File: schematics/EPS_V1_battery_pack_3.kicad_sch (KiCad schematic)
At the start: 31 parts, among them U10 MP2672AGD-0000-Z, U11 MAX17205G+

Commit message: Fix NC pins, add 2 test points & silkscreen labels
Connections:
- net GND: now also U10.14 (SCL), U10.15 (SDA), U11.10 (AIN2), U11.9 (AIN1)
- no-connect marks 6 -> 2
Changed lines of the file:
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@@
 	)
 	(junction
+		(at 229.87 87.63)
+		(diameter 0)
+		(color 0 0 0 0)
+	)
+	(junction
+		(at 104.14 91.44)
+		(diameter 0)
+		(color 0 0 0 0)
+	)
+	(junction
 		(at 196.85 101.6)
 		(diameter 0)
@@
 	)
 	(junction
+		(at 104.14 88.9)
+		(diameter 0)
+		(color 0 0 0 0)
+	)
+	(junction
 		(at 58.42 67.31)
 		(diameter 0)
@@
 	)
 	(no_connect
-		(at 104.14 88.9)
-	)
-	(no_connect
-		(at 229.87 90.17)
-	)
-	(no_connect
-		(at 104.14 86.36)
-	)
-	(no_connect
 		(at 229.87 77.47)
 	)
-	(no_connect
-		(at 229.87 87.63)
-	)
 	(wire
 		(pts
@@
 	(wire
 		(pts
-			(xy 229.87 92.71) (xy 231.14 92.71)
-		)
-		(stroke
-			(width 0)
-			(type default)
-		)
-	)
-	(wire
-		(pts
 			(xy 104.14 81.28) (xy 116.84 81.28)
 		)
@@
 	(wire
 		(pts
+			(xy 229.87 95.25) (xy 229.87 92.71)
+		)
+		(stroke
+			(width 0)
+			(type default)
+		)
+	)
+	(wire
+		(pts
 			(xy 121.92 68.58) (xy 121.92 63.5)
 		)
@@
 	(wire
 		(pts
+			(xy 104.14 88.9) (xy 104.14 91.44)
+		)
+		(stroke
+			(width 0)
+			(type default)
+		)
+	)
+	(wire
+		(pts
 			(xy 267.97 82.55) (xy 265.43 82.55)
 		)
@@
 	(wire
 		(pts
+			(xy 229.87 95.25) (xy 232.41 95.25)
+		)
+		(stroke
+			(width 0)
+			(type default)
+		)
+	)
+	(wire
+		(pts
 			(xy 62.23 81.28) (xy 63.5 81.28)
 		)
@@
 	(wire
 		(pts
+			(xy 229.87 87.63) (xy 229.87 90.17)
+		)
+		(stroke
+			(width 0)
+			(type default)
+		)
+	)
+	(wire
+		(pts
 			(xy 118.11 104.14) (xy 120.65 104.14)
 		)
@@
 	(wire
 		(pts
+			(xy 104.14 86.36) (xy 104.14 88.9)
+		)
+		(stroke
+			(width 0)
+			(type default)
+		)
+	)
+	(wire
+		(pts
 			(xy 45.72 91.44) (xy 45.72 106.68)
 		)
@@
 	(wire
 		(pts
+			(xy 229.87 87.63) (xy 233.68 87.63)
+		)
+		(stroke
+			(width 0)
+			(type default)
+		)
+	)
+	(wire
+		(pts
 			(xy 100.33 106.68) (xy 104.14 106.68)
 		)
@@
 		)
 	)
-	(global_label "ALRT"
-		(shape output)
-		(at 231.14 92.71 0)
-		(fields_autoplaced yes)
-		(effects
-			(font
-				(size 1.27 1.27)
-			)
-			(justify left)
-		)
-		(property "Intersheetrefs" "${INTERSHEET_REFS}"
-			(at 238.4795 92.71 0)
-			(hide yes)
-			(show_name no)
-			(do_not_autoplace no)
-			(effects
-				(font
-					(size 1.27 1.27)
-				)
-				(justify left)
-			)
-		)
-	)
 	(global_label "BATT3+"
 		(shape passive)
@@
 		)
 	)
+	(global_label "ALRT"
+		(shape output)
+		(at 232.41 95.25 0)
+		(fields_autoplaced yes)
+		(effects
+			(font
+				(size 1.27 1.27)
+			)
+			(justify left)
+		)
+		(property "Intersheetrefs" "${INTERSHEET_REFS}"
+			(at 239.7495 95.25 0)
+			(hide yes)
+			(show_name no)
+			(do_not_autoplace no)
+			(effects
+				(font
+					(size 1.27 1.27)
+				)
+				(justify left)
+			)
+		)
+	)
 	(global_label "BATT3+"
 		(shape passive)
@@
 	)
 	(symbol
-		(lib_id "power:GND")
-		(at 232.41 100.33 0)
-		(unit 1)
-		(body_style 1)
-		(exclude_from_sim no)
-		(in_bom yes)
-		(on_board yes)
-		(in_pos_files yes)
-		(dnp no)
-		(property "Reference" "#PWR0100"
-			(at 232.41 106.68 0)
-			(hide yes)
-			(show_name no)
-			(do_not_autoplace no)
-			(effects
-				(font
-					(size 1.27 1.27)
-				)
-			)
-		)
-		(property "Value" "GND"
-			(at 232.41 104.394 0)
-			(show_name no)
-			(do_not_autoplace no)
-			(effects
-				(font
-					(size 1.27 1.27)
-				)
-			)
-		)
-		(property "Footprint" ""
-			(at 232.41 100.33 0)
-			(hide yes)
-			(show_name no)
-			(do_not_autoplace no)
-			(effects
-				(font
-					(size 1.27 1.27)
-				)
-			)
-		)
-		(property "Datasheet" ""
-			(at 232.41 100.33 0)
-			(hide yes)
-			(show_name no)
-			(do_not_autoplace no)
-			(effects
-				(font
-					(size 1.27 1.27)
-				)
-			)
-		)
-		(property "Description" "Power symbol creates a global label with name \"GND\" , ground"
-			(at 232.41 100.33 0)
-			(hide yes)
-			(show_name no)
-			(do_not_autoplace no)
-			(effects
-				(font
-					(size 1.27 1.27)
-				)
-			)
-		)
-		(pin "1"
-		)
-		(instances
-			(project "EPS_V1"
-				(path "/85157432-5d03-48fa-ab40-27ed3d133f47/eb164b0c-5007-4f8f-b822-af0e1d9e197d"
-					(reference "#PWR0100")
-					(unit 1)
-				)
-			)
-		)
-	)
-	(symbol
 		(lib_id "Device:R_US")
 		(at 205.74 101.6 270)
@@
 					(unit 1)
 				)
+			)
+		)
+	)
+	(symbol
+		(lib_id "power:GND")
+		(at 233.68 87.63 0)
+		(unit 1)
+		(body_style 1)
+		(exclude_from_sim no)
+		(in_bom yes)
+		(on_board yes)
+		(in_pos_files yes)
+		(dnp no)
+		(property "Reference" "#PWR0132"
+			(at 233.68 93.98 0)
+			(hide yes)
+			(show_name no)
+			(do_not_autoplace no)
+			(effects
+				(font
+					(size 1.27 1.27)
+				)
+			)
+		)
+		(property "Value" "GND"
+			(at 233.68 91.694 0)
+			(show_name no)
+			(do_not_autoplace no)
+			(effects
+				(font
+					(size 1.27 1.27)
+				)
+			)
+		)
+		(property "Footprint" ""
+			(at 233.68 87.63 0)
+			(hide yes)
+			(show_name no)
+			(do_not_autoplace no)
+			(effects
+				(font
+					(size 1.27 1.27)
+				)
+			)
+		)
+		(property "Datasheet" ""
+			(at 233.68 87.63 0)
+			(hide yes)
+			(show_name no)
+			(do_not_autoplace no)
+			(effects
+				(font
+					(size 1.27 1.27)
+				)
+			)
+		)
+		(property "Description" "Power symbol creates a global label with name \"GND\" , ground"
+			(at 233.68 87.63 0)
+			(hide yes)
+			(show_name no)
+			(do_not_autoplace no)
+			(effects
+				(font
+					(size 1.27 1.27)
+				)
+			)
+		)
+		(pin "1"
+		)
+		(instances
+			(project "EPS_V1"
+				(path "/85157432-5d03-48fa-ab40-27ed3d133f47/eb164b0c-5007-4f8f-b822-af0e1d9e197d"
+					(reference "#PWR0132")
+					(unit 1)
+				)

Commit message: Fix silkscreen; Fix component value style
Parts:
- C_BATT6, C_BST3: value 0.1u -> 100n
- C_REG6, C_REG7: value 0.47u -> 470n
- R_BATT3, R_MID3: value 50 -> 50R
- R_SCL3, R_SDA3: value 150 -> 150R
- R_SENSE3: value 0.01 -> 10m
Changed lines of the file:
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@@
 			)
 		)
-		(property "Value" "0.1u"
+		(property "Value" "100n"
 			(at 167.132 87.63 0)
 			(show_name no)
@@
 			)
 		)
-		(property "Value" "50"
+		(property "Value" "50R"
 			(at 61.722 101.6 0)
 			(show_name no)
@@
 			)
 		)
-		(property "Value" "0.47u"
+		(property "Value" "470n"
 			(at 172.212 100.33 0)
 			(show_name no)
@@
 			)
 		)
-		(property "Value" "0.01"
+		(property "Value" "10m"
 			(at 201.676 106.934 90)
 			(show_name no)
@@
 			)
 		)
-		(property "Value" "150"
+		(property "Value" "150R"
 			(at 247.904 89.916 90)
 			(show_name no)
@@
 			)
 		)
-		(property "Value" "0.1u"
+		(property "Value" "100n"
 			(at 55.118 78.74 0)
 			(show_name no)
@@
 			)
 		)
-		(property "Value" "50"
+		(property "Value" "50R"
 			(at 165.354 80.264 90)
 			(show_name no)
@@
 			)
 		)
-		(property "Value" "0.47u"
+		(property "Value" "470n"
 			(at 182.118 115.57 0)
 			(show_name no)
@@
 			)
 		)
-		(property "Value" "150"
+		(property "Value" "150R"
 			(at 263.144 77.724 90)
 			(show_name no)

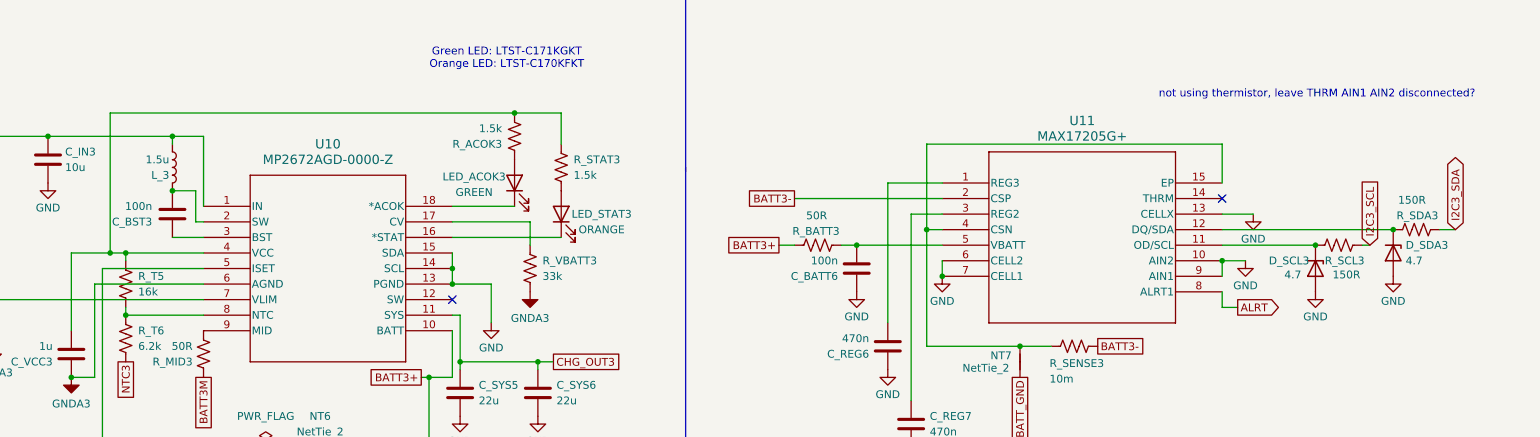
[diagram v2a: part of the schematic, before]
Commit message: Switch out MP28167 for LTC3119 (MPPC buck-boost) in schematic
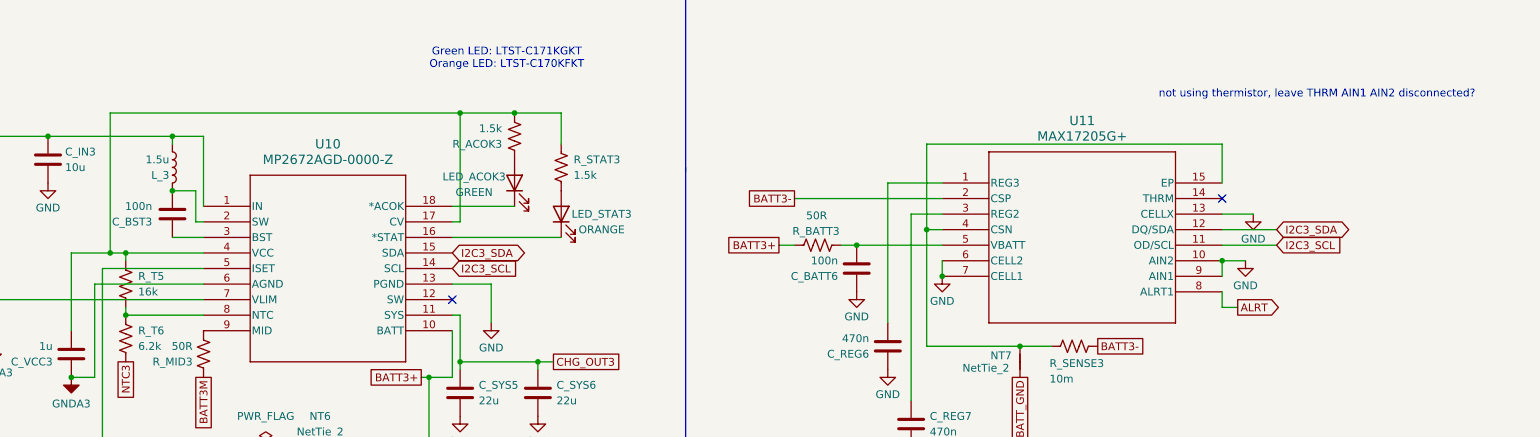
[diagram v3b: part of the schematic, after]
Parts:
- removed D_SCL3, D_SDA3: 4.7, Diode_SMD:D_0603_1608Metric, symbol Device:D_Zener
- removed R_SCL3, R_SDA3: 150R, Resistor_SMD:R_0603_1608Metric, symbol Device:R_US
- removed R_VBATT3: 33k, Resistor_SMD:R_0603_1608Metric, symbol Device:R_US
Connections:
- net GND: no longer U10.14 (SCL), U10.15 (SDA)
- net I2C3_SCL: now also U10.14 (SCL), U11.11 (OD/SCL)
- net I2C3_SDA: now also U10.15 (SDA), U11.12 (DQ/SDA)
- net at C_VCC3.2, R_ACOK3.2, R_STAT3.1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: now also U10.17 (CV)

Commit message: fix U6 EN pin, add ALRT pullup R, update 3dmodels, regen step
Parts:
- R_ISET3: value 6k -> 24k
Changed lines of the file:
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@@
 			)
 		)
-		(property "Value" "6k"
+		(property "Value" "24k"
 			(at 48.768 129.54 0)
 			(show_name no)
